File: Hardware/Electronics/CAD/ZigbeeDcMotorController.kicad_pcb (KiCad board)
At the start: 2 copper layers, 45 x 20 mm, 13 parts, among them J1 Conn_01x02, J3 Conn_01x02, J4 Conn_01x04, J5 Conn_01x07, K1 AZ832P2-x, Q1 BC846, Q3 BC846

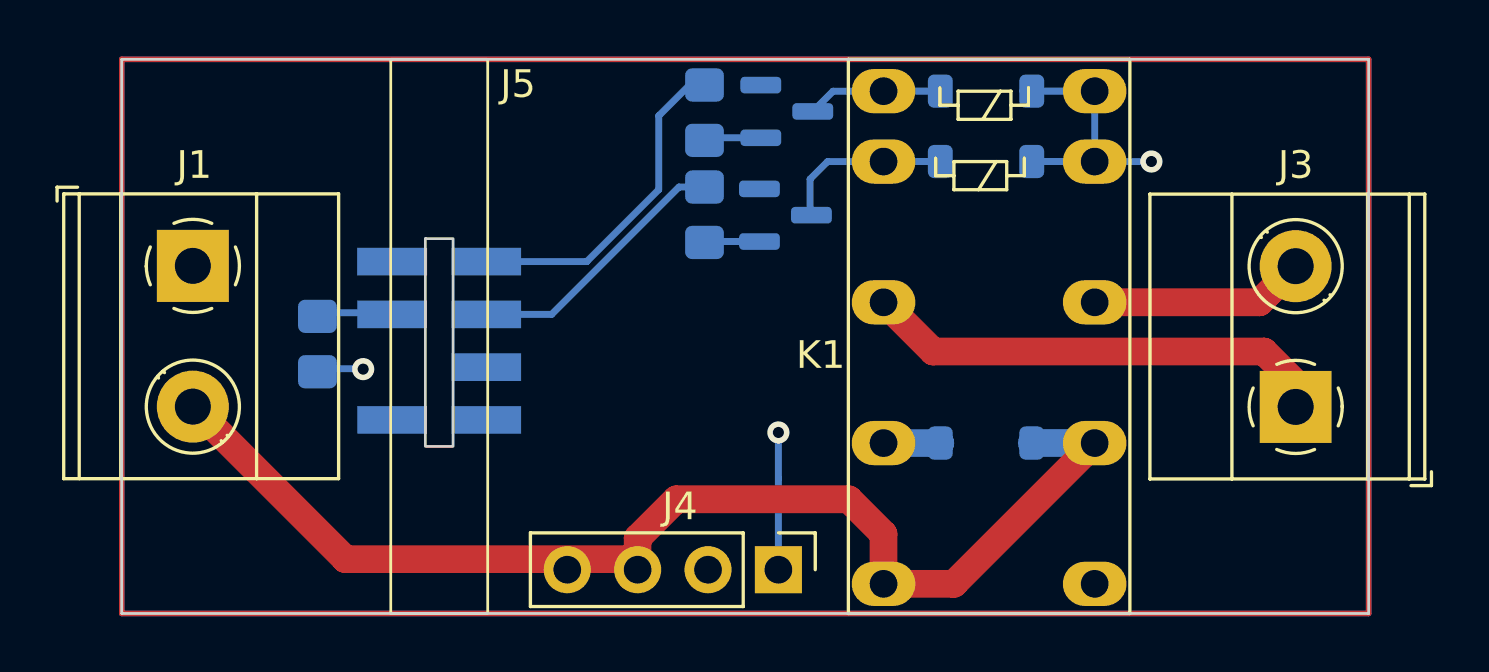
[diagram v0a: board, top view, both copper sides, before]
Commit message: Second design with LDO
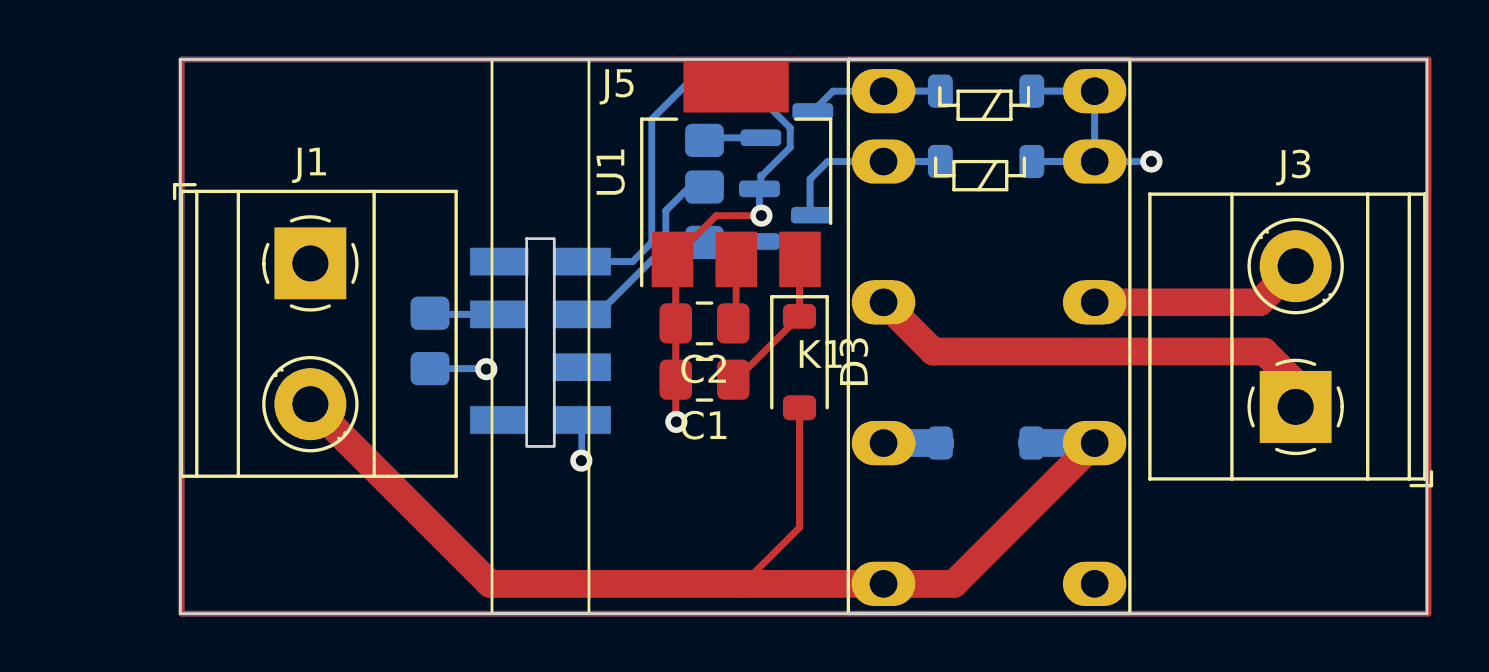
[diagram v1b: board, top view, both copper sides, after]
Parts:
- removed J4: Conn_01x04, Connector_PinHeader_2.54mm:PinHeader_1x04_P2.54mm_Vertical
- added C1: C, Capacitor_SMD:C_0805_2012Metric_Pad1.18x1.45mm_HandSolder, F.Cu at (121.0, 51.6)
- added C2: C, Capacitor_SMD:C_0805_2012Metric_Pad1.18x1.45mm_HandSolder, F.Cu at (121.0, 49.5)
- added D3: 1N4148W, Diode_SMD:D_SOD-123, F.Cu at (124.5, 50.9)
- added U1: NCP1117-3.3_SOT223, Package_TO_SOT_SMD:SOT-223-3_TabPin2, F.Cu at (122.2, 44.1)
- moved J1 4.24 mm to (106.8, 47.4)
- moved R3 4.07 mm to (111.1, 50.2)
- moved J5 3.65 mm to (115.1, 49.8)
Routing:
- net GND: track 2.05 -> 17.5 mm, vias 0 -> 2
- net Net-(D3-K): track 0.00 -> 5.40 mm
- net Reset: track 9.78 -> 6.87 mm
- net Set: track 12.1 -> 9.46 mm
